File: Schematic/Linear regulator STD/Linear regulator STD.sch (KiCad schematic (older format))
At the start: 0 parts

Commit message: schematic alpha
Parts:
- added C1: 100nF, symbol Device:C
- added C2: 100uF, symbol Device:CP
- added C3: 10uF, symbol Device:CP
- added D1, D2: 1N4002, symbol Device:D
- added R1, R2: R, symbol Device:R
- added U?: LM317DCYR, digikey-footprints:SOT-223-4, symbol dk_PMIC-Voltage-Regulators-Linear:LM317DCYR
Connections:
- net labels added: GND, VIN, VOUT
- wire segments 0 -> 33
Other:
- note added: "VO = ((R2 / R1) + 1) * 1.25\n\nhttps://github.com/oshw-dev/Linear-regulator-STD/wiki\n\n3.28V R1 = 240, R2 = 390\n5.04V R1 = 330, R2 = 1000\n11.83V R1 = 390, R2 = 3300\n"
- note added: "place near LM317"
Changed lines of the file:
@@
 Comment4 ""
 $EndDescr
+$Comp
+L dk_PMIC-Voltage-Regulators-Linear:LM317DCYR U?
+U 1 1 5CCEED29
+P 5950 2900
+F 0 "U?" H 5950 3187 60  0000 C CNN
+F 1 "LM317DCYR" H 5950 3081 60  0000 C CNN
+F 2 "digikey-footprints:SOT-223-4" H 6150 3100 60  0001 L CNN
+F 3 "http://www.ti.com/general/docs/suppproductinfo.tsp?distId=10&gotoUrl=http%3A%2F%2Fwww.ti.com%2Flit%2Fgpn%2Flm317" H 6150 3200 60  0001 L CNN
+F 4 "296-12602-1-ND" H 6150 3300 60  0001 L CNN "Digi-Key_PN"
+F 5 "LM317DCYR" H 6150 3400 60  0001 L CNN "MPN"
+F 6 "Integrated Circuits (ICs)" H 6150 3500 60  0001 L CNN "Category"
+F 7 "PMIC - Voltage Regulators - Linear" H 6150 3600 60  0001 L CNN "Family"
+F 8 "http://www.ti.com/general/docs/suppproductinfo.tsp?distId=10&gotoUrl=http%3A%2F%2Fwww.ti.com%2Flit%2Fgpn%2Flm317" H 6150 3700 60  0001 L CNN "DK_Datasheet_Link"
+F 9 "/product-detail/en/texas-instruments/LM317DCYR/296-12602-1-ND/443738" H 6150 3800 60  0001 L CNN "DK_Detail_Page"
+F 10 "IC REG LIN POS ADJ 1.5A SOT223-4" H 6150 3900 60  0001 L CNN "Description"
+F 11 "Texas Instruments" H 6150 4000 60  0001 L CNN "Manufacturer"
+F 12 "Active" H 6150 4100 60  0001 L CNN "Status"
+	1    5950 2900
+	1    0    0    -1
+$EndComp
+Text Notes 5050 1950 0    50   ~ 0
+VO = ((R2 / R1) + 1) * 1.25\n\nhttps://github.com/oshw-dev/Linear-regulator-STD/wiki\n\n3.28V R1 = 240, R2 = 390\n5.04V R1 = 330, R2 = 1000\n11.83V R1 = 390, R2 = 3300\n
+$Comp
+L Device:R R1
+U 1 1 5CCF23F9
+P 6850 3250
+F 0 "R1" H 6920 3296 50  0000 L CNN
+F 1 "R" H 6920 3205 50  0000 L CNN
+F 2 "" V 6780 3250 50  0001 C CNN
+F 3 "~" H 6850 3250 50  0001 C CNN
+	1    6850 3250
+	1    0    0    -1
+$EndComp
+$Comp
+L Device:R R2
+U 1 1 5CCF3D73
+P 6850 3650
+F 0 "R2" H 6920 3696 50  0000 L CNN
+F 1 "R" H 6920 3605 50  0000 L CNN
+F 2 "" V 6780 3650 50  0001 C CNN
+F 3 "~" H 6850 3650 50  0001 C CNN
+	1    6850 3650
+	1    0    0    -1
+$EndComp
+$Comp
+L power:GND #PWR?
+U 1 1 5CCF4CA5
+P 5950 4000
+F 0 "#PWR?" H 5950 3750 50  0001 C CNN
+F 1 "GND" H 5955 3827 50  0000 C CNN
+F 2 "" H 5950 4000 50  0001 C CNN
+F 3 "" H 5950 4000 50  0001 C CNN
+	1    5950 4000
+	1    0    0    -1
+$EndComp
+Wire Wire Line
+	6250 3000 6350 3000
+Wire Wire Line
+	5950 3450 5950 3200
+$Comp
+L Device:C C1
+U 1 1 5CCF7777
+P 5350 3350
+F 0 "C1" H 5465 3396 50  0000 L CNN
+F 1 "100nF" H 5465 3305 50  0000 L CNN
+F 2 "" H 5388 3200 50  0001 C CNN
+F 3 "~" H 5350 3350 50  0001 C CNN
+	1    5350 3350
+	1    0    0    -1
+$EndComp
+Connection ~ 5950 3900
+Wire Wire Line
+	5000 2900 5350 2900
+Wire Wire Line
+	5350 3200 5350 2900
+Connection ~ 5350 2900
+Wire Wire Line
+	5350 2900 5650 2900
+Wire Wire Line
+	5000 3900 5350 3900
+Wire Wire Line
+	5350 3500 5350 3900
+Connection ~ 5350 3900
+Wire Wire Line
+	5350 3900 5950 3900
+Text Notes 5200 3700 1    50   ~ 0
+place near LM317
+Text Label 7300 2900 0    50   ~ 0
+VOUT
+Text Label 4850 2900 0    50   ~ 0
+VIN
+Text Label 7300 3900 0    50   ~ 0
+GND
+Text Label 4850 3900 0    50   ~ 0
+GND
+$Comp
+L Device:D D1
+U 1 1 5CCFBD45
+P 5950 2350
+F 0 "D1" H 5950 2566 50  0000 C CNN
+F 1 "1N4002" H 5950 2475 50  0000 C CNN
+F 2 "" H 5950 2350 50  0001 C CNN
+F 3 "~" H 5950 2350 50  0001 C CNN
+	1    5950 2350
+	1    0    0    -1
+$EndComp
+Wire Wire Line
+	5800 2350 5350 2350
+Wire Wire Line
+	5350 2350 5350 2900
+$Comp
+L Device:D D2
+U 1 1 5CCFDCF5
+P 6350 3250
+F 0 "D2" V 6304 3329 50  0000 L CNN
+F 1 "1N4002" V 6395 3329 50  0000 L CNN
+F 2 "" H 6350 3250 50  0001 C CNN
+F 3 "~" H 6350 3250 50  0001 C CNN
+	1    6350 3250
+	0    1    1    0
+$EndComp
+Wire Wire Line
+	6350 3400 6350 3450
+Connection ~ 6350 3450
+Wire Wire Line
+	6350 3450 5950 3450
+Wire Wire Line
+	6350 3100 6350 3000
+Wire Wire Line
+	6250 2900 6350 2900
+Wire Wire Line
+	6850 3450 6850 3400
+Wire Wire Line
+	6350 3450 6850 3450
+Wire Wire Line
+	6850 3500 6850 3450
+Connection ~ 6850 3450
+Wire Wire Line
+	6850 3800 6850 3900
+Connection ~ 6850 3900
+Wire Wire Line
+	6850 3900 7150 3900
+Connection ~ 6850 2900
+Wire Wire Line
+	6850 2900 7150 2900
+Wire Wire Line
+	6850 2350 6850 2900
+Wire Wire Line
+	6100 2350 6850 2350
+Wire Wire Line
+	6850 2900 6850 3100
+Wire Wire Line
+	6350 3000 6350 2900
+Connection ~ 6350 3000
+Connection ~ 6350 2900
+Wire Wire Line
+	6350 2900 6850 2900
+$Comp
+L Device:CP C2
+U 1 1 5CD0148C
+P 7150 3450
+F 0 "C2" H 7268 3496 50  0000 L CNN
+F 1 "100uF" H 7268 3405 50  0000 L CNN
+F 2 "" H 7188 3300 50  0001 C CNN
+F 3 "~" H 7150 3450 50  0001 C CNN
+	1    7150 3450
+	1    0    0    -1
+$EndComp
+Wire Wire Line
+	7150 2900 7150 3300
+Connection ~ 7150 2900
+Wire Wire Line
+	7150 2900 7300 2900
+Wire Wire Line
+	7150 3600 7150 3900
+Connection ~ 7150 3900
+Wire Wire Line
+	7150 3900 7300 3900
+$Comp
+L Device:CP C3
+U 1 1 5CD032FA
+P 5950 3650
+F 0 "C3" H 6068 3696 50  0000 L CNN
+F 1 "10uF" H 6068 3605 50  0000 L CNN
+F 2 "" H 5988 3500 50  0001 C CNN
+F 3 "~" H 5950 3650 50  0001 C CNN
+	1    5950 3650
+	1    0    0    -1
+$EndComp
+Wire Wire Line
+	5950 3900 5950 4000
+Wire Wire Line
+	5950 3900 6850 3900
+Wire Wire Line
+	5950 3800 5950 3900
+Wire Wire Line
+	5950 3500 5950 3450
+Connection ~ 5950 3450
 $EndSCHEMATC

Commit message: schematic alpha
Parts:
- C1: footprint (none) -> Capacitor_SMD:C_0603_1608Metric_Pad1.05x0.95mm_HandSolder; Description (none) -> >=50V
- C2: value 100uF -> 47uF
- gave numbers to parts that had none: 1
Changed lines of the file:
@@
 $EndDescr
 $Comp
-L dk_PMIC-Voltage-Regulators-Linear:LM317DCYR U?
+L dk_PMIC-Voltage-Regulators-Linear:LM317DCYR U1
 U 1 1 5CCEED29
 P 5950 2900
-F 0 "U?" H 5950 3187 60  0000 C CNN
+F 0 "U1" H 5950 3187 60  0000 C CNN
 F 1 "LM317DCYR" H 5950 3081 60  0000 C CNN
 F 2 "digikey-footprints:SOT-223-4" H 6150 3100 60  0001 L CNN
@@
 $EndComp
 $Comp
-L power:GND #PWR?
+L power:GND #PWR0101
 U 1 1 5CCF4CA5
 P 5950 4000
-F 0 "#PWR?" H 5950 3750 50  0001 C CNN
+F 0 "#PWR0101" H 5950 3750 50  0001 C CNN
 F 1 "GND" H 5955 3827 50  0000 C CNN
 F 2 "" H 5950 4000 50  0001 C CNN
@@
 F 0 "C1" H 5465 3396 50  0000 L CNN
 F 1 "100nF" H 5465 3305 50  0000 L CNN
-F 2 "" H 5388 3200 50  0001 C CNN
+F 2 "Capacitor_SMD:C_0603_1608Metric_Pad1.05x0.95mm_HandSolder" H 5388 3200 50  0001 C CNN
 F 3 "~" H 5350 3350 50  0001 C CNN
+F 4 ">=50V" H 0   0   50  0001 C CNN "Description"
 	1    5350 3350
 	1    0    0    -1
@@
 P 7150 3450
 F 0 "C2" H 7268 3496 50  0000 L CNN
-F 1 "100uF" H 7268 3405 50  0000 L CNN
+F 1 "47uF" H 7268 3405 50  0000 L CNN
 F 2 "" H 7188 3300 50  0001 C CNN
 F 3 "~" H 7150 3450 50  0001 C CNN

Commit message: Annotation (alpha)
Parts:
- C2: footprint (none) -> Capacitor_SMD:CP_Elec_6.3x5.8
- C3: footprint (none) -> Capacitor_SMD:CP_Elec_4x5.4
- D1, D2: footprint (none) -> Diode_SMD:D_SOD-123F
- R1, R2: footprint (none) -> Resistor_SMD:R_0603_1608Metric_Pad1.05x0.95mm_HandSolder
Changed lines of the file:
@@
 F 0 "R1" H 6920 3296 50  0000 L CNN
 F 1 "R" H 6920 3205 50  0000 L CNN
-F 2 "" V 6780 3250 50  0001 C CNN
+F 2 "Resistor_SMD:R_0603_1608Metric_Pad1.05x0.95mm_HandSolder" V 6780 3250 50  0001 C CNN
 F 3 "~" H 6850 3250 50  0001 C CNN
 	1    6850 3250
@@
 F 0 "R2" H 6920 3696 50  0000 L CNN
 F 1 "R" H 6920 3605 50  0000 L CNN
-F 2 "" V 6780 3650 50  0001 C CNN
+F 2 "Resistor_SMD:R_0603_1608Metric_Pad1.05x0.95mm_HandSolder" V 6780 3650 50  0001 C CNN
 F 3 "~" H 6850 3650 50  0001 C CNN
 	1    6850 3650
@@
 F 0 "D1" H 5950 2566 50  0000 C CNN
 F 1 "1N4002" H 5950 2475 50  0000 C CNN
-F 2 "" H 5950 2350 50  0001 C CNN
-F 3 "~" H 5950 2350 50  0001 C CNN
+F 2 "Diode_SMD:D_SOD-123F" H 5950 2350 50  0001 C CNN
+F 3 "https://datasheet.lcsc.com/szlcsc/Shandong-Jingdao-Microelectronics-1N4002W_C169542.pdf" H 5950 2350 50  0001 C CNN
 	1    5950 2350
 	1    0    0    -1
@@
 F 0 "D2" V 6304 3329 50  0000 L CNN
 F 1 "1N4002" V 6395 3329 50  0000 L CNN
-F 2 "" H 6350 3250 50  0001 C CNN
-F 3 "~" H 6350 3250 50  0001 C CNN
+F 2 "Diode_SMD:D_SOD-123F" H 6350 3250 50  0001 C CNN
+F 3 "https://datasheet.lcsc.com/szlcsc/Shandong-Jingdao-Microelectronics-1N4002W_C169542.pdf" H 6350 3250 50  0001 C CNN
 	1    6350 3250
 	0    1    1    0
@@
 F 0 "C2" H 7268 3496 50  0000 L CNN
 F 1 "47uF" H 7268 3405 50  0000 L CNN
-F 2 "" H 7188 3300 50  0001 C CNN
-F 3 "~" H 7150 3450 50  0001 C CNN
+F 2 "Capacitor_SMD:CP_Elec_6.3x5.8" H 7188 3300 50  0001 C CNN
+F 3 "https://datasheet.lcsc.com/szlcsc/PANASONIC-EEHZA1V470P_C178639.pdf" H 7150 3450 50  0001 C CNN
 	1    7150 3450
 	1    0    0    -1
@@
 F 0 "C3" H 6068 3696 50  0000 L CNN
 F 1 "10uF" H 6068 3605 50  0000 L CNN
-F 2 "" H 5988 3500 50  0001 C CNN
-F 3 "~" H 5950 3650 50  0001 C CNN
+F 2 "Capacitor_SMD:CP_Elec_4x5.4" H 5988 3500 50  0001 C CNN
+F 3 "https://datasheet.lcsc.com/szlcsc/1901071210_PANASONIC-EEE1VA100WAR_C336731.pdf" H 5950 3650 50  0001 C CNN
 	1    5950 3650
 	1    0    0    -1

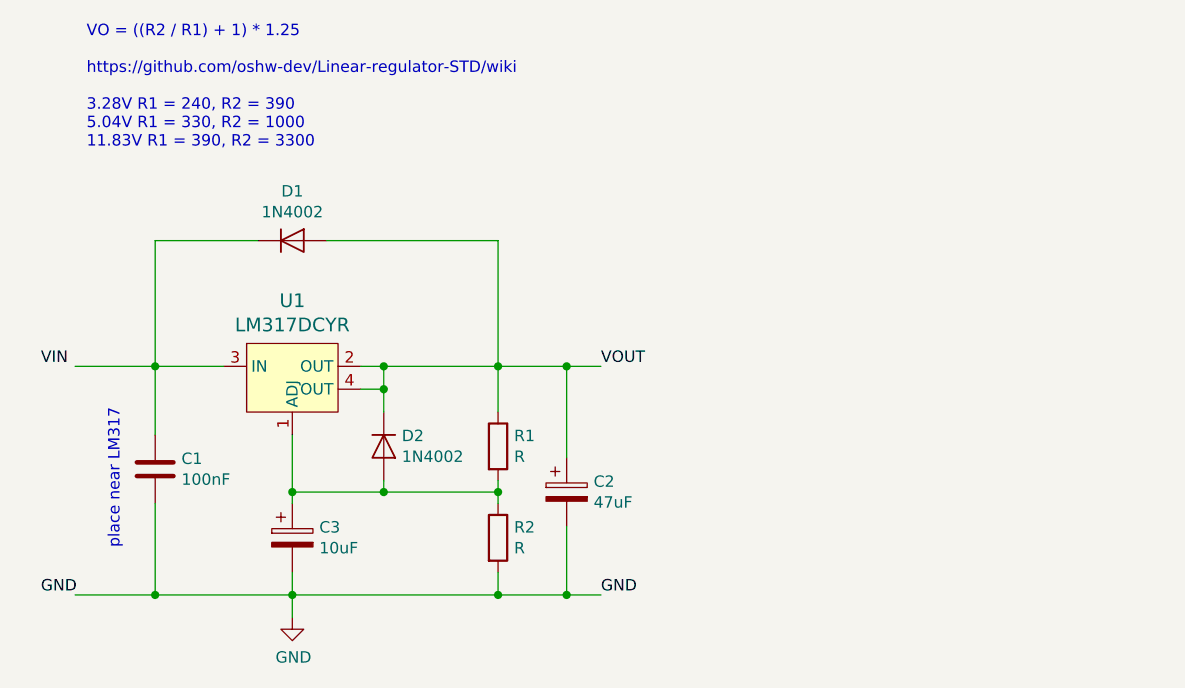
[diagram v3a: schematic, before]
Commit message: TO220 package, C1 & c3 caps updated to 22uF Tantalum, C3 10uF ceramic
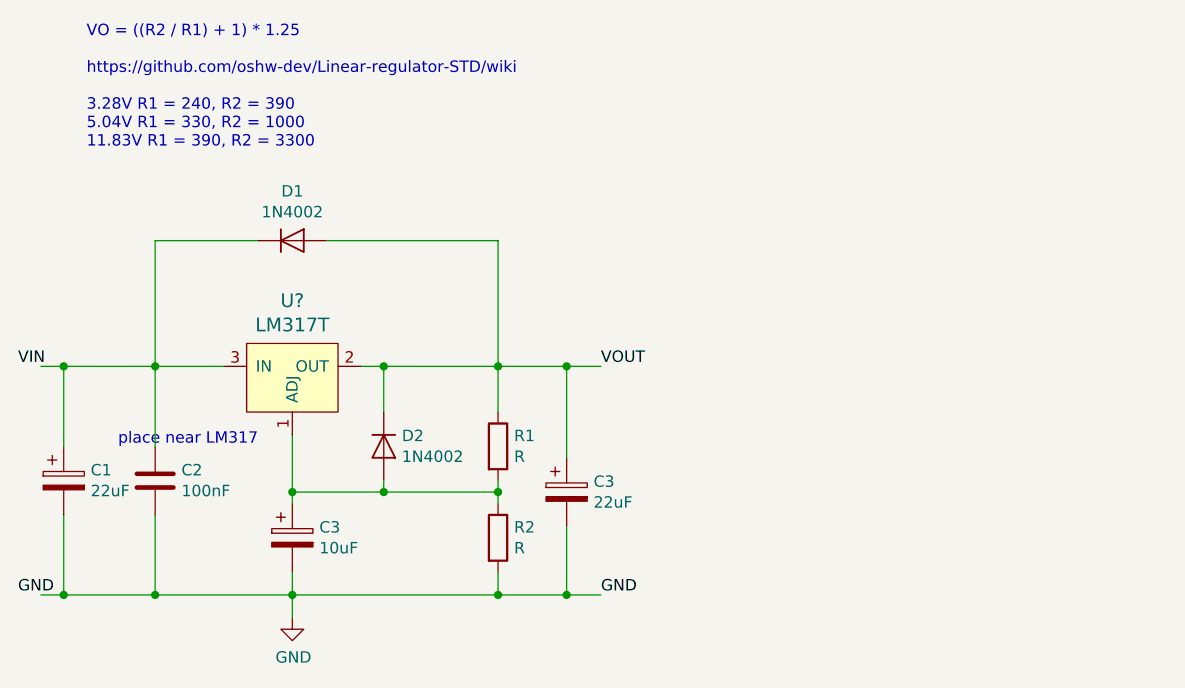
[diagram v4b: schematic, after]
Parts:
- removed U1: LM317DCYR, digikey-footprints:SOT-223-4, symbol dk_PMIC-Voltage-Regulators-Linear:LM317DCYR
- added C1: 22uF, Capacitor_Tantalum_SMD:CP_EIA-3528-15_AVX-H_Pad1.50x2.35mm_HandSolder, symbol Device:CP
- added U?: LM317T, digikey-footprints:TO-220-3, symbol dk_PMIC-Voltage-Regulators-Linear:LM317T
- C3: renamed from C2; value 47uF -> 22uF; footprint Capacitor_SMD:CP_Elec_6.3x5.8 -> Capacitor_Tantalum_SMD:CP_EIA-3528-15_AVX-H_Pad1.50x2.35mm_HandSolder
- C3: footprint Capacitor_SMD:CP_Elec_4x5.4 -> Capacitor_SMD:C_1206_3216Metric_Pad1.42x1.75mm_HandSolder
- renumbered C1 to C2
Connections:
- wire segments 33 -> 35
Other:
- moved on the sheet: C2
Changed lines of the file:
@@
 Comment4 ""
 $EndDescr
-$Comp
-L dk_PMIC-Voltage-Regulators-Linear:LM317DCYR U1
-U 1 1 5CCEED29
-P 5950 2900
-F 0 "U1" H 5950 3187 60  0000 C CNN
-F 1 "LM317DCYR" H 5950 3081 60  0000 C CNN
-F 2 "digikey-footprints:SOT-223-4" H 6150 3100 60  0001 L CNN
-F 3 "http://www.ti.com/general/docs/suppproductinfo.tsp?distId=10&gotoUrl=http%3A%2F%2Fwww.ti.com%2Flit%2Fgpn%2Flm317" H 6150 3200 60  0001 L CNN
-F 4 "296-12602-1-ND" H 6150 3300 60  0001 L CNN "Digi-Key_PN"
-F 5 "LM317DCYR" H 6150 3400 60  0001 L CNN "MPN"
-F 6 "Integrated Circuits (ICs)" H 6150 3500 60  0001 L CNN "Category"
-F 7 "PMIC - Voltage Regulators - Linear" H 6150 3600 60  0001 L CNN "Family"
-F 8 "http://www.ti.com/general/docs/suppproductinfo.tsp?distId=10&gotoUrl=http%3A%2F%2Fwww.ti.com%2Flit%2Fgpn%2Flm317" H 6150 3700 60  0001 L CNN "DK_Datasheet_Link"
-F 9 "/product-detail/en/texas-instruments/LM317DCYR/296-12602-1-ND/443738" H 6150 3800 60  0001 L CNN "DK_Detail_Page"
-F 10 "IC REG LIN POS ADJ 1.5A SOT223-4" H 6150 3900 60  0001 L CNN "Description"
-F 11 "Texas Instruments" H 6150 4000 60  0001 L CNN "Manufacturer"
-F 12 "Active" H 6150 4100 60  0001 L CNN "Status"
-	1    5950 2900
-	1    0    0    -1
-$EndComp
 Text Notes 5050 1950 0    50   ~ 0
 VO = ((R2 / R1) + 1) * 1.25\n\nhttps://github.com/oshw-dev/Linear-regulator-STD/wiki\n\n3.28V R1 = 240, R2 = 390\n5.04V R1 = 330, R2 = 1000\n11.83V R1 = 390, R2 = 3300\n
@@
 $EndComp
 Wire Wire Line
-	6250 3000 6350 3000
-Wire Wire Line
 	5950 3450 5950 3200
 $Comp
-L Device:C C1
+L Device:C C2
 U 1 1 5CCF7777
-P 5350 3350
-F 0 "C1" H 5465 3396 50  0000 L CNN
-F 1 "100nF" H 5465 3305 50  0000 L CNN
-F 2 "Capacitor_SMD:C_0603_1608Metric_Pad1.05x0.95mm_HandSolder" H 5388 3200 50  0001 C CNN
-F 3 "~" H 5350 3350 50  0001 C CNN
-F 4 ">=50V" H 0   0   50  0001 C CNN "Description"
-	1    5350 3350
+P 5350 3400
+F 0 "C2" H 5465 3446 50  0000 L CNN
+F 1 "100nF" H 5465 3355 50  0000 L CNN
+F 2 "Capacitor_SMD:C_0603_1608Metric_Pad1.05x0.95mm_HandSolder" H 5388 3250 50  0001 C CNN
+F 3 "~" H 5350 3400 50  0001 C CNN
+F 4 ">=50V" H 0   50  50  0001 C CNN "Description"
+	1    5350 3400
 	1    0    0    -1
 $EndComp
 Connection ~ 5950 3900
-Wire Wire Line
-	5000 2900 5350 2900
-Wire Wire Line
-	5350 3200 5350 2900
 Connection ~ 5350 2900
 Wire Wire Line
 	5350 2900 5650 2900
-Wire Wire Line
-	5000 3900 5350 3900
-Wire Wire Line
-	5350 3500 5350 3900
-Connection ~ 5350 3900
-Wire Wire Line
-	5350 3900 5950 3900
-Text Notes 5200 3700 1    50   ~ 0
+Text Notes 5800 3250 2    50   ~ 0
 place near LM317
 Text Label 7300 2900 0    50   ~ 0
 VOUT
-Text Label 4850 2900 0    50   ~ 0
+Text Label 4750 2900 0    50   ~ 0
 VIN
 Text Label 7300 3900 0    50   ~ 0
 GND
-Text Label 4850 3900 0    50   ~ 0
+Text Label 4750 3900 0    50   ~ 0
 GND
 $Comp
@@
 	6350 3450 5950 3450
 Wire Wire Line
-	6350 3100 6350 3000
-Wire Wire Line
 	6250 2900 6350 2900
 Wire Wire Line
@@
 Wire Wire Line
 	6850 2900 6850 3100
-Wire Wire Line
-	6350 3000 6350 2900
-Connection ~ 6350 3000
 Connection ~ 6350 2900
 Wire Wire Line
 	6350 2900 6850 2900
 $Comp
-L Device:CP C2
+L Device:CP C3
 U 1 1 5CD0148C
 P 7150 3450
-F 0 "C2" H 7268 3496 50  0000 L CNN
-F 1 "47uF" H 7268 3405 50  0000 L CNN
-F 2 "Capacitor_SMD:CP_Elec_6.3x5.8" H 7188 3300 50  0001 C CNN
-F 3 "https://datasheet.lcsc.com/szlcsc/PANASONIC-EEHZA1V470P_C178639.pdf" H 7150 3450 50  0001 C CNN
+F 0 "C3" H 7268 3496 50  0000 L CNN
+F 1 "22uF" H 7268 3405 50  0000 L CNN
+F 2 "Capacitor_Tantalum_SMD:CP_EIA-3528-15_AVX-H_Pad1.50x2.35mm_HandSolder" H 7188 3300 50  0001 C CNN
+F 3 "https://datasheet.lcsc.com/szlcsc/AVX-TAJB226K020RNJ_C7199.pdf" H 7150 3450 50  0001 C CNN
 	1    7150 3450
 	1    0    0    -1
@@
 F 0 "C3" H 6068 3696 50  0000 L CNN
 F 1 "10uF" H 6068 3605 50  0000 L CNN
-F 2 "Capacitor_SMD:CP_Elec_4x5.4" H 5988 3500 50  0001 C CNN
-F 3 "https://datasheet.lcsc.com/szlcsc/1901071210_PANASONIC-EEE1VA100WAR_C336731.pdf" H 5950 3650 50  0001 C CNN
+F 2 "Capacitor_SMD:C_1206_3216Metric_Pad1.42x1.75mm_HandSolder" H 5988 3500 50  0001 C CNN
+F 3 "https://datasheet.lcsc.com/szlcsc/Samsung-Electro-Mechanics-CL31B106KAHNNNE_C14860.pdf" H 5950 3650 50  0001 C CNN
 	1    5950 3650
 	1    0    0    -1
@@
 	5950 3500 5950 3450
 Connection ~ 5950 3450
+$Comp
+L dk_PMIC-Voltage-Regulators-Linear:LM317T U?
+U 1 1 5CD0B04B
+P 5950 2900
+F 0 "U?" H 5950 3187 60  0000 C CNN
+F 1 "LM317T" H 5950 3081 60  0000 C CNN
+F 2 "digikey-footprints:TO-220-3" H 6150 3100 60  0001 L CNN
+F 3 "http://www.st.com/content/ccc/resource/technical/document/datasheet/group1/a0/db/e6/9b/6f/9c/45/7b/CD00000455/files/CD00000455.pdf/jcr:content/translations/en.CD00000455.pdf" H 6150 3200 60  0001 L CNN
+F 4 "497-1575-5-ND" H 6150 3300 60  0001 L CNN "Digi-Key_PN"
+F 5 "LM317T" H 6150 3400 60  0001 L CNN "MPN"
+F 6 "Integrated Circuits (ICs)" H 6150 3500 60  0001 L CNN "Category"
+F 7 "PMIC - Voltage Regulators - Linear" H 6150 3600 60  0001 L CNN "Family"
+F 8 "http://www.st.com/content/ccc/resource/technical/document/datasheet/group1/a0/db/e6/9b/6f/9c/45/7b/CD00000455/files/CD00000455.pdf/jcr:content/translations/en.CD00000455.pdf" H 6150 3700 60  0001 L CNN "DK_Datasheet_Link"
+F 9 "/product-detail/en/stmicroelectronics/LM317T/497-1575-5-ND/591677" H 6150 3800 60  0001 L CNN "DK_Detail_Page"
+F 10 "IC REG LIN POS ADJ 1.5A TO220AB" H 6150 3900 60  0001 L CNN "Description"
+F 11 "STMicroelectronics" H 6150 4000 60  0001 L CNN "Manufacturer"
+F 12 "Active" H 6150 4100 60  0001 L CNN "Status"
+	1    5950 2900
+	1    0    0    -1
+$EndComp
+Wire Wire Line
+	6350 2900 6350 3100
+Wire Wire Line
+	5350 2900 5350 3250
+Wire Wire Line
+	5350 3550 5350 3900
+Connection ~ 5350 3900
+Wire Wire Line
+	5350 3900 5950 3900
+Wire Wire Line
+	4850 2900 4950 2900
+Wire Wire Line
+	4850 3900 4950 3900
+$Comp
+L Device:CP C1
+U 1 1 5CD11A37
+P 4950 3400
+F 0 "C1" H 5068 3446 50  0000 L CNN
+F 1 "22uF" H 5068 3355 50  0000 L CNN
+F 2 "Capacitor_Tantalum_SMD:CP_EIA-3528-15_AVX-H_Pad1.50x2.35mm_HandSolder" H 4988 3250 50  0001 C CNN
+F 3 "https://datasheet.lcsc.com/szlcsc/AVX-TAJB226K020RNJ_C7199.pdf" H 4950 3400 50  0001 C CNN
+	1    4950 3400
+	1    0    0    -1
+$EndComp
+Wire Wire Line
+	4950 3250 4950 2900
+Connection ~ 4950 2900
+Wire Wire Line
+	4950 2900 5350 2900
+Wire Wire Line
+	4950 3550 4950 3900
+Connection ~ 4950 3900
+Wire Wire Line
+	4950 3900 5350 3900
 $EndSCHEMATC

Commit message: Update Linear regulator STD.sch
C3 name duplicate fix
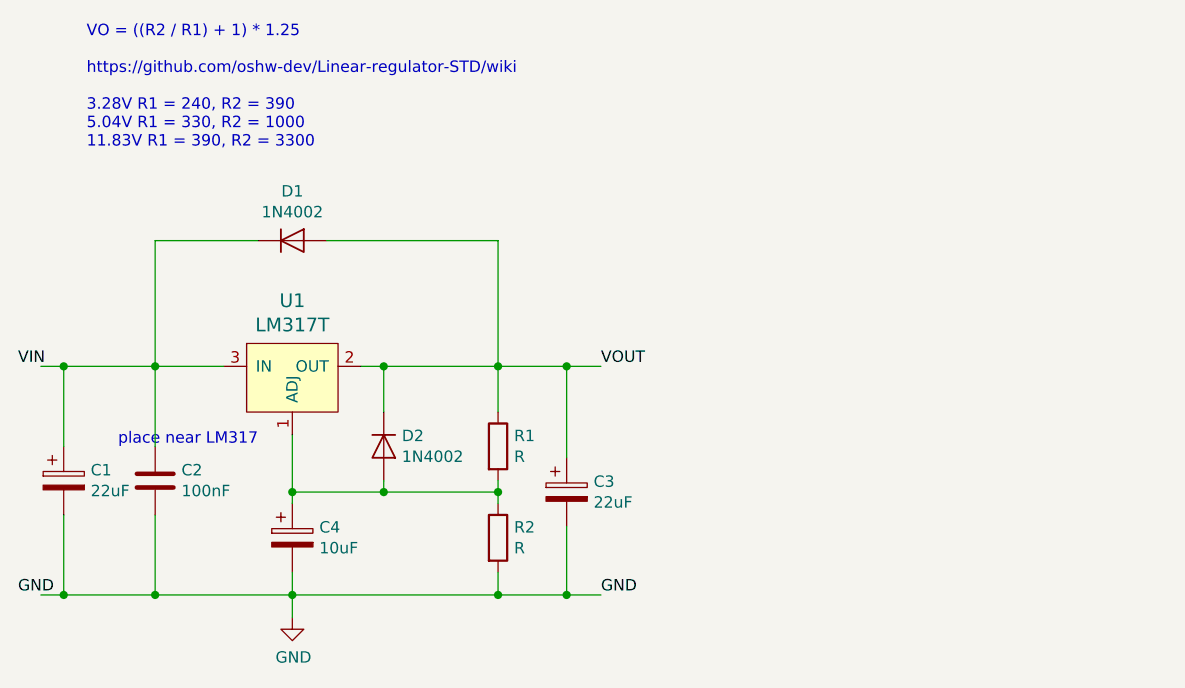
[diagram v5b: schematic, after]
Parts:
- gave numbers to parts that had none: 1
- renumbered C3 to C4
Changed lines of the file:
@@
 	7150 3900 7300 3900
 $Comp
-L Device:CP C3
+L Device:CP C4
 U 1 1 5CD032FA
 P 5950 3650
-F 0 "C3" H 6068 3696 50  0000 L CNN
+F 0 "C4" H 6068 3696 50  0000 L CNN
 F 1 "10uF" H 6068 3605 50  0000 L CNN
 F 2 "Capacitor_SMD:C_1206_3216Metric_Pad1.42x1.75mm_HandSolder" H 5988 3500 50  0001 C CNN
@@
 Connection ~ 5950 3450
 $Comp
-L dk_PMIC-Voltage-Regulators-Linear:LM317T U?
+L dk_PMIC-Voltage-Regulators-Linear:LM317T U1
 U 1 1 5CD0B04B
 P 5950 2900
-F 0 "U?" H 5950 3187 60  0000 C CNN
+F 0 "U1" H 5950 3187 60  0000 C CNN
 F 1 "LM317T" H 5950 3081 60  0000 C CNN
 F 2 "digikey-footprints:TO-220-3" H 6150 3100 60  0001 L CNN
